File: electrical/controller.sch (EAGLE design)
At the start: 36 parts, among them IC1 MCP6232, IC2 LTC1661MSOP8, IC3 MCP6232, IC4 ICM7555, IC5 CD40109B, Q1 DMP3098, Q3 600mA/40V, U1 U3V16F15, U2 U3V16F15

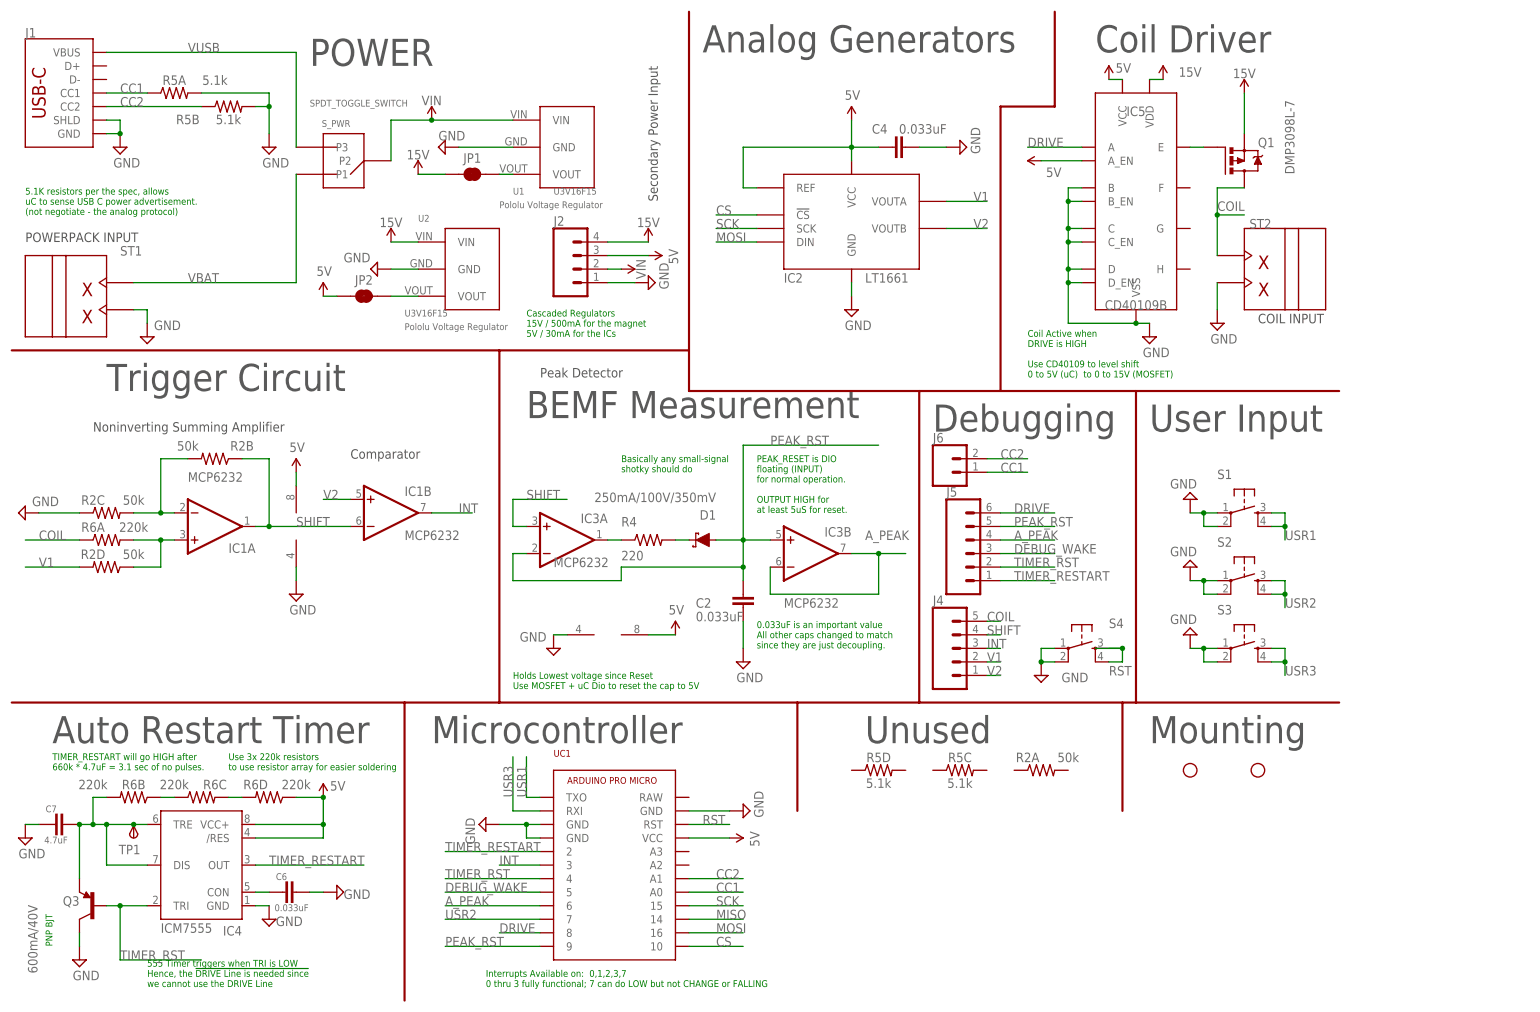
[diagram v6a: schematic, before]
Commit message: Fix many erratta, overhaul power planes
Rev D4 now WIP.
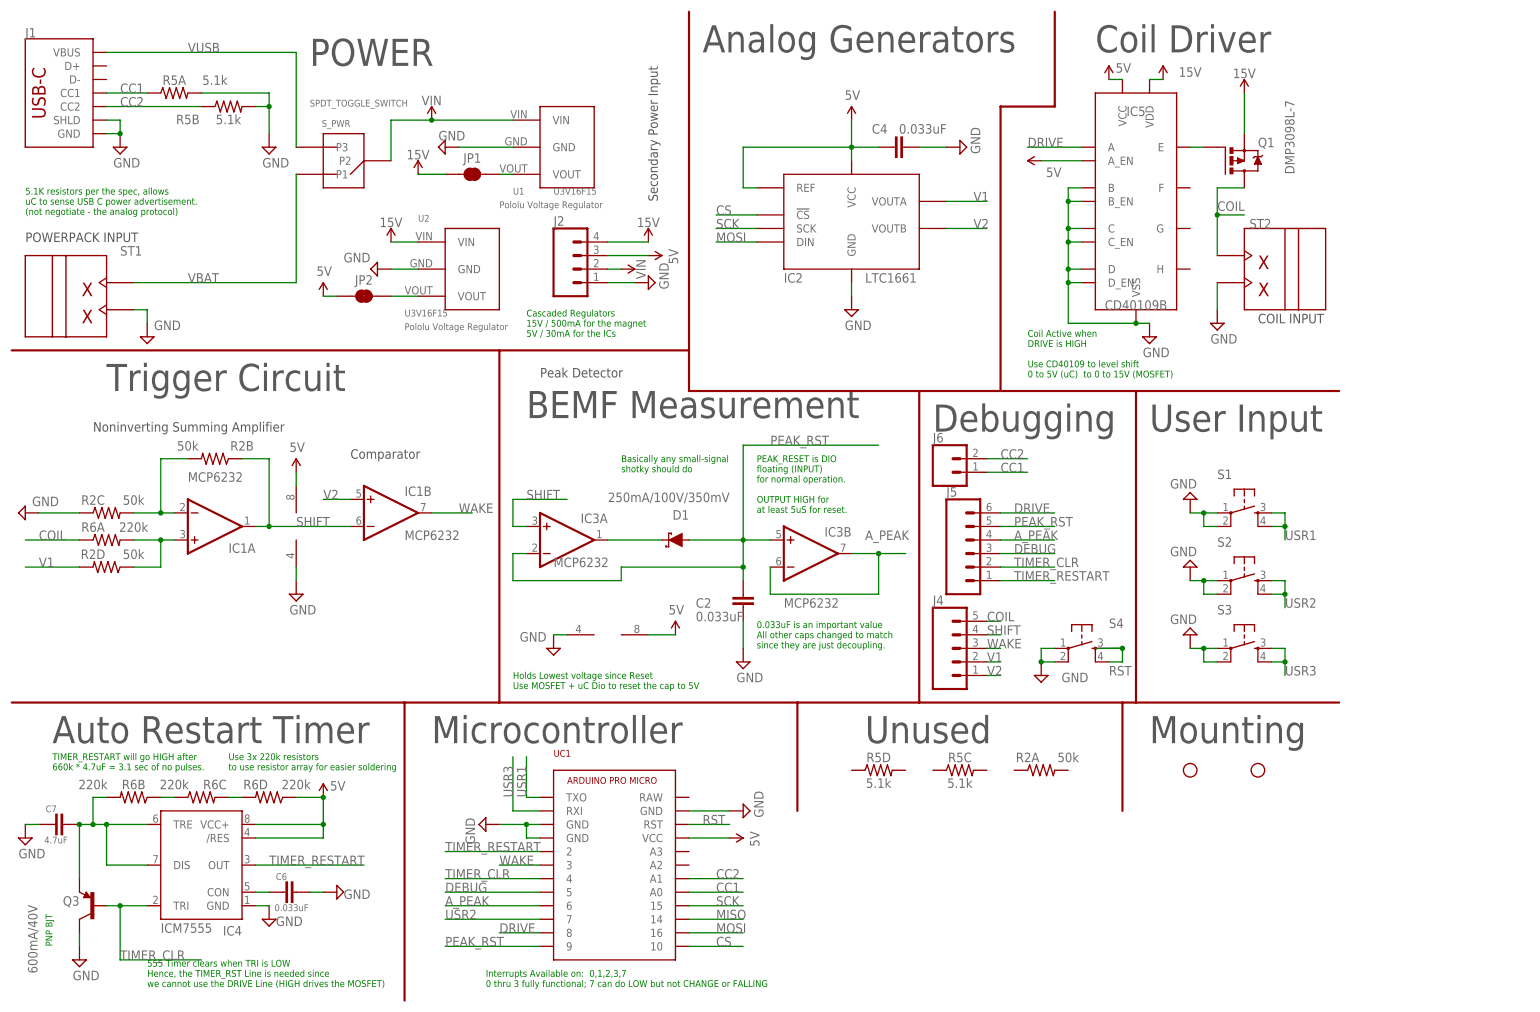
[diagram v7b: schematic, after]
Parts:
- removed R4: 220, BEST_Custom:R-US_R0603
- removed TP1: TPSPAD1-13, testpad:TPSPAD1-13
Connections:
- net DEBUG_WAKE renamed DEBUG
- net INT renamed WAKE
- net TIMER_RST renamed TIMER_CLR
- removed net N$2: IC3A.OUT, R4.1
- net N$1: now also IC3A.OUT; no longer R4.2
- net N$7: no longer TP1.PP
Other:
- note added: "555 Timer clears when TRI is LOW Hence, the TIMER_RST Line is needed since we cannot use the DRIVE Line (HIGH drives the MOSFET)"
- note added: "Stage 2: VShift = 1 + (R4/R3) V- Choose R4=R3=50k (for part unification) VShift = 2 V-"
- note removed: "555 Timer triggers when TRI is LOW Hence, the !DRIVE Line is needed since we cannot use the DRIVE Line"
- note removed: "Stage 2: VShift = 1 + (R4/R3) V- Choose R4=R3=22k (for part unification) VShift = 2 V-"
- moved on the sheet: D1
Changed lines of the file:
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@@
 <parts>
 <part name="FRAME1" library="pie" deviceset="FRAME_SCHEMATIC" device="">
-<attribute name="REVISION" value="D3"/>
+<attribute name="REVISION" value="D4"/>
 </part>
 <part name="UC1" library="BEST_Custom" library_urn="urn:adsk.eagle:library:10805467" deviceset="ARDUINO_PRO_MICRO" device="USBC" package3d_urn="urn:adsk.eagle:package:49279263/1"/>
@@
 <part name="JP1" library="SparkFun-Jumpers" deviceset="JUMPER-SMT_2_NC_TRACE" device="_SILK" package3d_urn="urn:adsk.eagle:package:39281/1"/>
 <part name="JP2" library="SparkFun-Jumpers" deviceset="JUMPER-SMT_2_NC_TRACE" device="_SILK" package3d_urn="urn:adsk.eagle:package:39281/1"/>
-<part name="R4" library="BEST_Custom" library_urn="urn:adsk.eagle:library:10805467" deviceset="R-US_" device="R0603" package3d_urn="urn:adsk.eagle:package:10805838/1" value="220"/>
 <part name="R5" library="BEST_Custom" library_urn="urn:adsk.eagle:library:10805467" deviceset="RESISTOR_ARRAY_(4)" device="-1206-1/16W-5%" package3d_urn="urn:adsk.eagle:package:49177701/2" value="5.1k"/>
 <part name="R6" library="BEST_Custom" library_urn="urn:adsk.eagle:library:10805467" deviceset="RESISTOR_ARRAY_(4)" device="-1206-1/16W-5%" package3d_urn="urn:adsk.eagle:package:49177701/2" value="220k"/>
@@
 <part name="IC2" library="BEST_Custom" library_urn="urn:adsk.eagle:library:10805467" deviceset="LTC1661" device="MSOP8" package3d_urn="urn:adsk.eagle:package:49278251/2"/>
 <part name="SUPPLY9" library="pie" deviceset="GND" device=""/>
-<part name="TP1" library="testpad" library_urn="urn:adsk.eagle:library:385" deviceset="TPS" device="PAD1-13" package3d_urn="urn:adsk.eagle:package:27946/1" value="TPSPAD1-13"/>
 <part name="J5" library="SparkFun-Connectors" library_urn="urn:adsk.eagle:library:49052309" deviceset="CONN_06" device="NO_SILK_NO_POP" package3d_urn="urn:adsk.eagle:package:49053105/1"/>
 <part name="J6" library="SparkFun-Connectors" library_urn="urn:adsk.eagle:library:49052309" deviceset="CONN_02" device="1X02_NO_SILK" package3d_urn="urn:adsk.eagle:package:49052902/1"/>
@@
 Use CD40109 to level shift
 0 to 5V (uC)  to 0 to 15V (MOSFET)</text>
-<text x="25.4" y="2.54" size="1.27" layer="91">555 Timer triggers when TRI is LOW
-Hence, the !DRIVE Line is needed since
-we cannot use the DRIVE Line</text>
+<text x="25.4" y="2.54" size="1.27" layer="91">555 Timer clears when TRI is LOW
+Hence, the TIMER_RST Line is needed since
+we cannot use the DRIVE Line (HIGH drives the MOSFET)</text>
 <text x="7.62" y="48.26" size="5.08" layer="97">Auto Restart Timer</text>
 <wire x1="147.32" y1="55.88" x2="170.18" y2="55.88" width="0.4064" layer="94"/>
@@
 <text x="55.88" y="63.5" size="1.27" layer="98">Stage 2:
 VShift = 1 + (R4/R3) V-
-Choose R4=R3=22k (for part unification)
+Choose R4=R3=50k (for part unification)
 VShift = 2 V-</text>
 <text x="66.04" y="76.2" size="1.27" layer="98">Stage 3:
@@
 <attribute name="VALUE" x="135.89" y="59.69" size="1.778" layer="96"/>
 </instance>
-<instance part="D1" gate="G$1" x="129.54" y="86.36" smashed="yes" rot="R180">
-<attribute name="NAME" x="132.08" y="91.948" size="1.778" layer="95" font="vector" rot="R180"/>
-<attribute name="VALUE" x="132.08" y="93.472" size="1.778" layer="96" font="vector" rot="R180" align="top-left"/>
+<instance part="D1" gate="G$1" x="124.46" y="86.36" smashed="yes" rot="R180">
+<attribute name="NAME" x="127" y="91.948" size="1.778" layer="95" font="vector" rot="R180"/>
+<attribute name="VALUE" x="134.62" y="93.472" size="1.778" layer="96" font="vector" rot="R180" align="top-left"/>
 </instance>
 <instance part="SUPPLY30" gate="G$1" x="114.3" y="137.16" smashed="yes" rot="R270">
@@
 <attribute name="NAME" x="66.04" y="135.128" size="1.778" layer="95" font="vector" align="center"/>
 </instance>
-<instance part="R4" gate="G$1" x="119.38" y="86.36" smashed="yes">
-<attribute name="NAME" x="114.3" y="88.9" size="1.778" layer="95"/>
-<attribute name="VALUE" x="114.3" y="82.55" size="1.778" layer="96"/>
-</instance>
 <instance part="R5" gate="A" x="30.48" y="170.18" smashed="yes">
 <attribute name="NAME" x="30.48" y="171.704" size="1.778" layer="95" font="vector" align="bottom-center"/>
@@
 <instance part="SUPPLY9" gate="GND" x="157.48" y="129.54" smashed="yes">
 <attribute name="VALUE" x="156.21" y="125.73" size="1.778" layer="96"/>
-</instance>
-<instance part="TP1" gate="G$1" x="22.86" y="30.48" smashed="yes" rot="R180">
-<attribute name="NAME" x="24.13" y="29.21" size="1.778" layer="95" rot="R180"/>
-<attribute name="TP_SIGNAL_NAME" x="21.59" y="31.75" size="1.778" layer="97" rot="R180"/>
 </instance>
 <instance part="J5" gate="J1" x="180.34" y="83.82" smashed="yes">
@@
 </segment>
 </net>
-<net name="INT" class="0">
+<net name="WAKE" class="0">
 <segment>
 <pinref part="IC1" gate="B" pin="OUT"/>
@@
 <pinref part="IC4" gate="G$1" pin="TRE"/>
 <wire x1="17.78" y1="25.4" x2="17.78" y2="33.02" width="0.1524" layer="91"/>
-<wire x1="17.78" y1="33.02" x2="22.86" y2="33.02" width="0.1524" layer="91"/>
+<wire x1="17.78" y1="33.02" x2="25.4" y2="33.02" width="0.1524" layer="91"/>
 <pinref part="C7" gate="G$1" pin="2"/>
-<wire x1="22.86" y1="33.02" x2="25.4" y2="33.02" width="0.1524" layer="91"/>
 <wire x1="12.7" y1="33.02" x2="15.24" y2="33.02" width="0.1524" layer="91"/>
 <junction x="17.78" y="33.02"/>
@@
 <pinref part="Q3" gate="G$1" pin="E"/>
 <wire x1="15.24" y1="33.02" x2="15.24" y2="38.1" width="0.1524" layer="91"/>
-<pinref part="TP1" gate="G$1" pin="PP"/>
-<junction x="22.86" y="33.02"/>
 <pinref part="R6" gate="B" pin="2"/>
 <wire x1="15.24" y1="38.1" x2="17.78" y2="38.1" width="0.1524" layer="91"/>
@@
 <wire x1="93.98" y1="83.82" x2="96.52" y2="83.82" width="0.1524" layer="91"/>
 <pinref part="D1" gate="G$1" pin="A"/>
-<wire x1="132.08" y1="86.36" x2="137.16" y2="86.36" width="0.1524" layer="91"/>
+<wire x1="127" y1="86.36" x2="137.16" y2="86.36" width="0.1524" layer="91"/>
 <junction x="137.16" y="86.36"/>
 <wire x1="137.16" y1="104.14" x2="137.16" y2="86.36" width="0.1524" layer="91"/>
@@
 </segment>
 </net>
-<net name="TIMER_RST" class="0">
+<net name="TIMER_CLR" class="0">
 <segment>
 <pinref part="IC4" gate="G$1" pin="TRI"/>
@@
 <net name="N$1" class="0">
 <segment>
-<pinref part="R4" gate="G$1" pin="2"/>
 <pinref part="D1" gate="G$1" pin="C"/>
-<wire x1="124.46" y1="86.36" x2="127" y2="86.36" width="0.1524" layer="91"/>
-</segment>
-</net>
-<net name="N$2" class="0">
-<segment>
-<pinref part="R4" gate="G$1" pin="1"/>
 <pinref part="IC3" gate="A" pin="OUT"/>
-<wire x1="114.3" y1="86.36" x2="111.76" y2="86.36" width="0.1524" layer="91"/>
+<wire x1="121.92" y1="86.36" x2="111.76" y2="86.36" width="0.1524" layer="91"/>
 </segment>
 </net>
@@
 </segment>
 </net>
-<net name="DEBUG_WAKE" class="0">
+<net name="DEBUG" class="0">
 <segment>
 <pinref part="J5" gate="J1" pin="3"/>

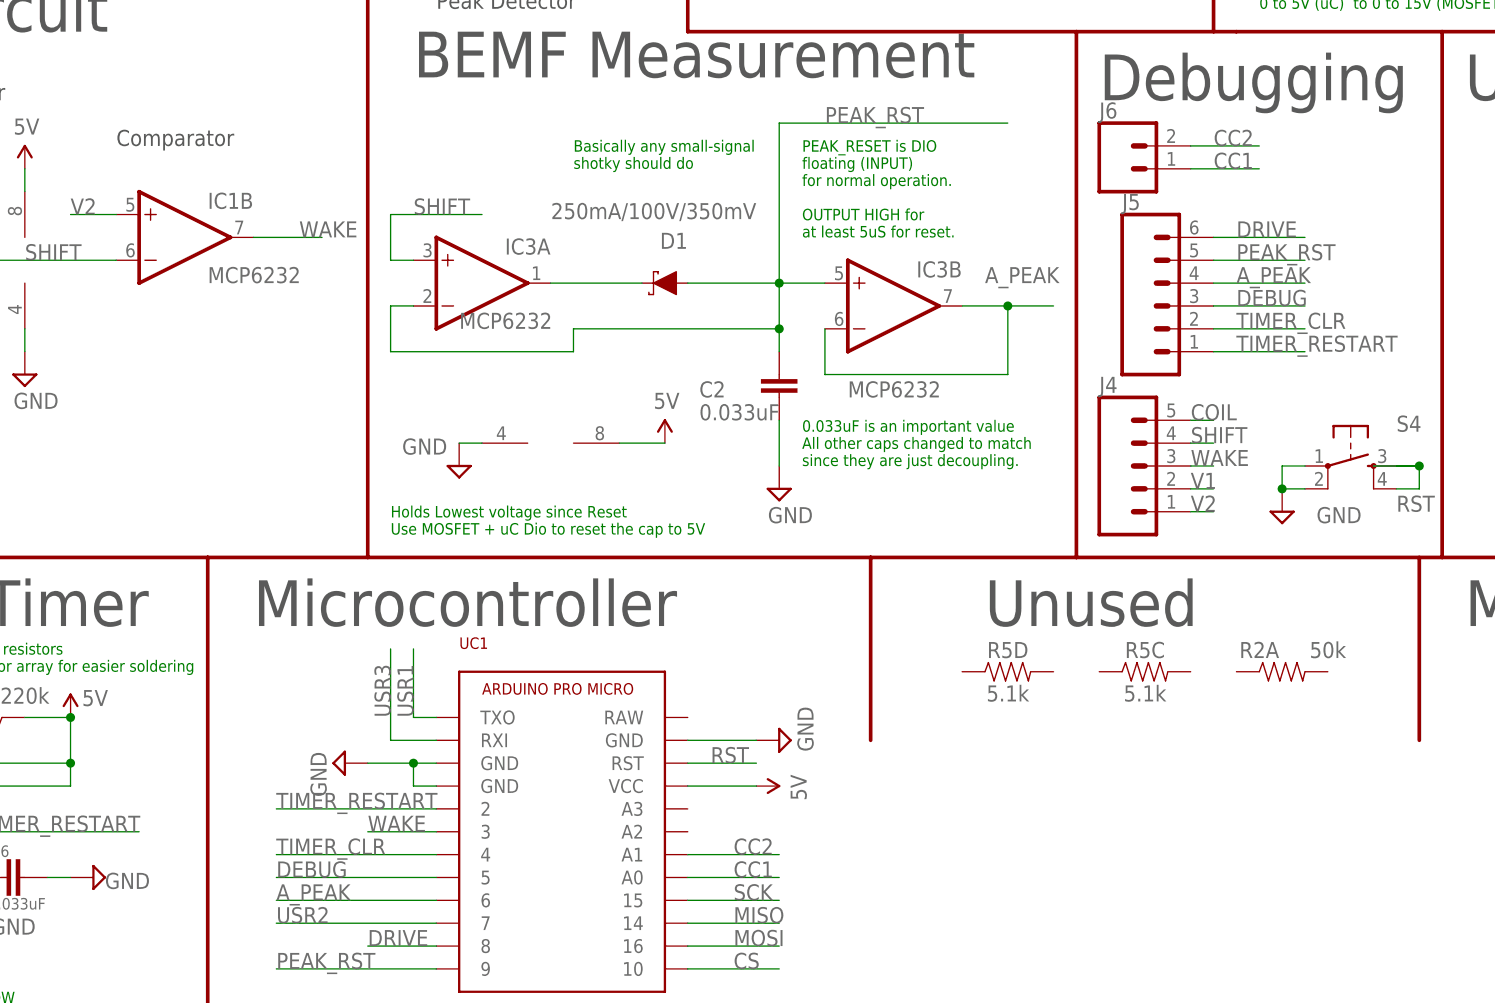
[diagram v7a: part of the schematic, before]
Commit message: Some pin renaming to make things easier to understand...
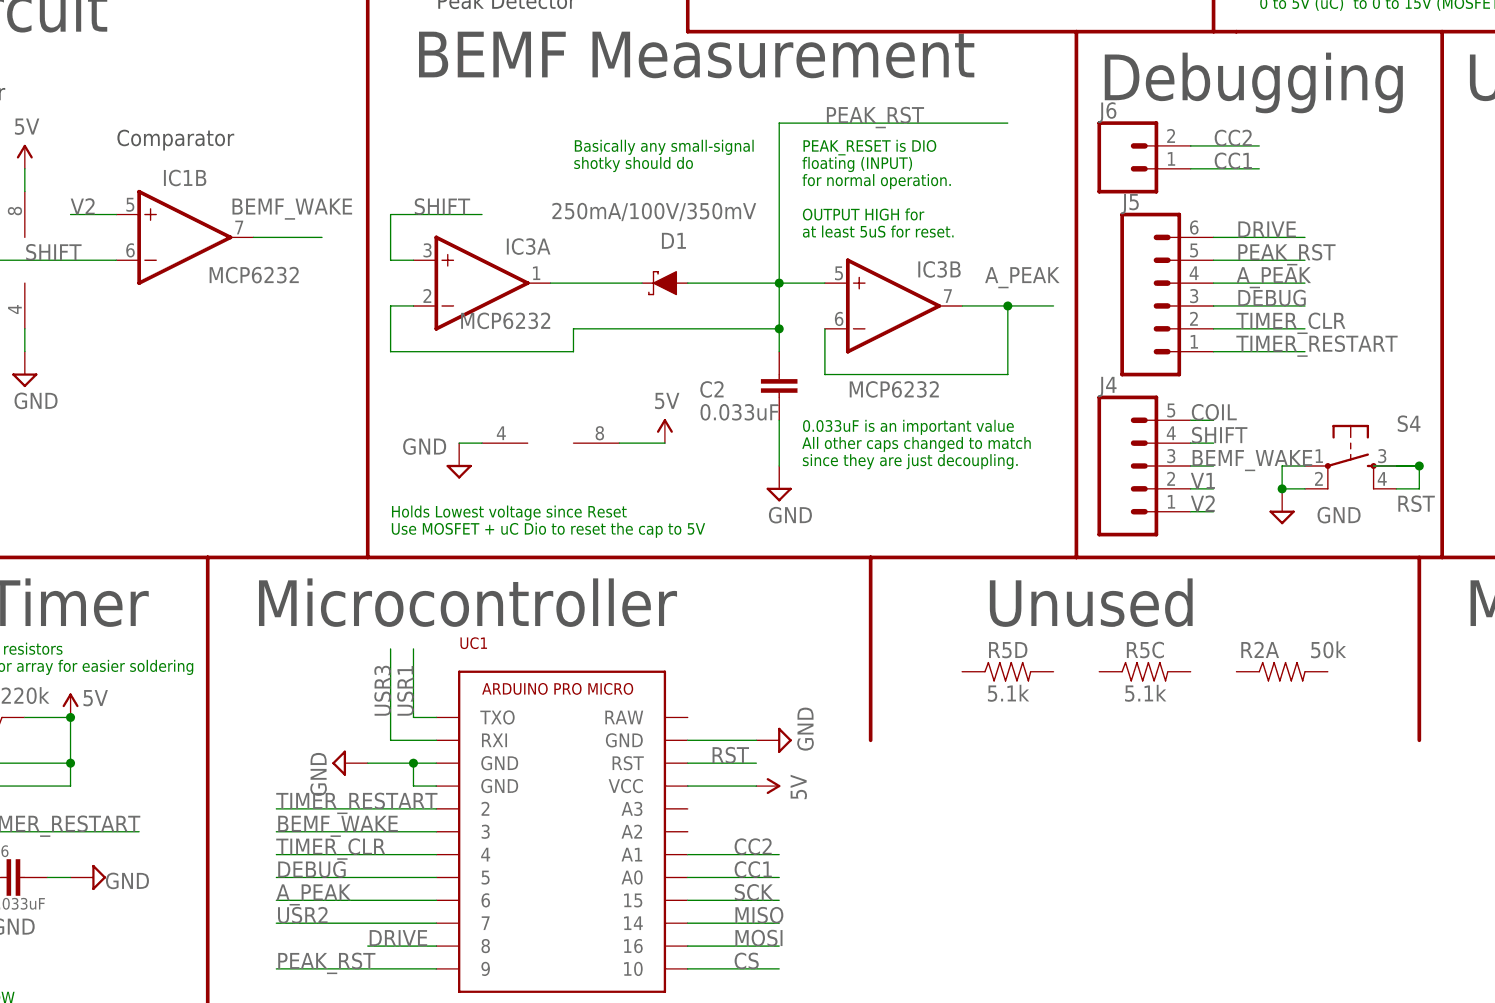
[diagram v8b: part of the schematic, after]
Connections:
- net WAKE renamed BEMF_WAKE
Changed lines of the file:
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@@
 <instance part="IC1" gate="P" x="53.34" y="88.9" smashed="yes"/>
 <instance part="IC1" gate="B" x="71.12" y="91.44" smashed="yes">
-<attribute name="NAME" x="73.66" y="94.615" size="1.778" layer="95"/>
+<attribute name="NAME" x="68.58" y="97.155" size="1.778" layer="95"/>
 <attribute name="VALUE" x="73.66" y="86.36" size="1.778" layer="96"/>
 </instance>
@@
 </segment>
 </net>
-<net name="WAKE" class="0">
-<segment>
-<pinref part="IC1" gate="B" pin="OUT"/>
-<wire x1="78.74" y1="91.44" x2="86.36" y2="91.44" width="0.1524" layer="91"/>
-<label x="83.82" y="91.44" size="1.778" layer="95"/>
-</segment>
-<segment>
-<pinref part="UC1" gate="APM" pin="3"/>
-<wire x1="99.06" y1="25.4" x2="91.44" y2="25.4" width="0.1524" layer="91"/>
-<label x="91.44" y="25.4" size="1.778" layer="95"/>
-</segment>
-<segment>
-<label x="182.88" y="66.04" size="1.778" layer="95"/>
-<pinref part="J4" gate="J1" pin="3"/>
-<wire x1="182.88" y1="66.04" x2="185.42" y2="66.04" width="0.1524" layer="91"/>
-</segment>
-</net>
 <net name="DRIVE" class="0">
 <segment>
@@
 </segment>
 </net>
+<net name="BEMF_WAKE" class="0">
+<segment>
+<pinref part="UC1" gate="APM" pin="3"/>
+<wire x1="99.06" y1="25.4" x2="81.28" y2="25.4" width="0.1524" layer="91"/>
+<label x="81.28" y="25.4" size="1.778" layer="95"/>
+</segment>
+<segment>
+<pinref part="IC1" gate="B" pin="OUT"/>
+<wire x1="78.74" y1="91.44" x2="86.36" y2="91.44" width="0.1524" layer="91"/>
+<label x="76.2" y="93.98" size="1.778" layer="95"/>
+</segment>
+<segment>
+<label x="182.88" y="66.04" size="1.778" layer="95"/>
+<pinref part="J4" gate="J1" pin="3"/>
+<wire x1="182.88" y1="66.04" x2="185.42" y2="66.04" width="0.1524" layer="91"/>
+</segment>
+</net>
